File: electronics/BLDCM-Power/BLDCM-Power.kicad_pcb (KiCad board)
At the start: 4 copper layers, 32 x 32 mm, 48 parts, among them J1 501920-3001, J2 53048-0310, J3 505578-0460, J4 505578-0460, J5 FTSH-107-01-L-DV-K, J6 12402012E212A, U1 INA240A1PWR, U2 LDLN030G33R, U3 TMC6300-LA, U4 INA240A1PWR, U5 TCAN1462, U6 INA240A1PWR, U7 BAT54S, U8 LDO40LPU50RY, U9 TPS2115ADRB

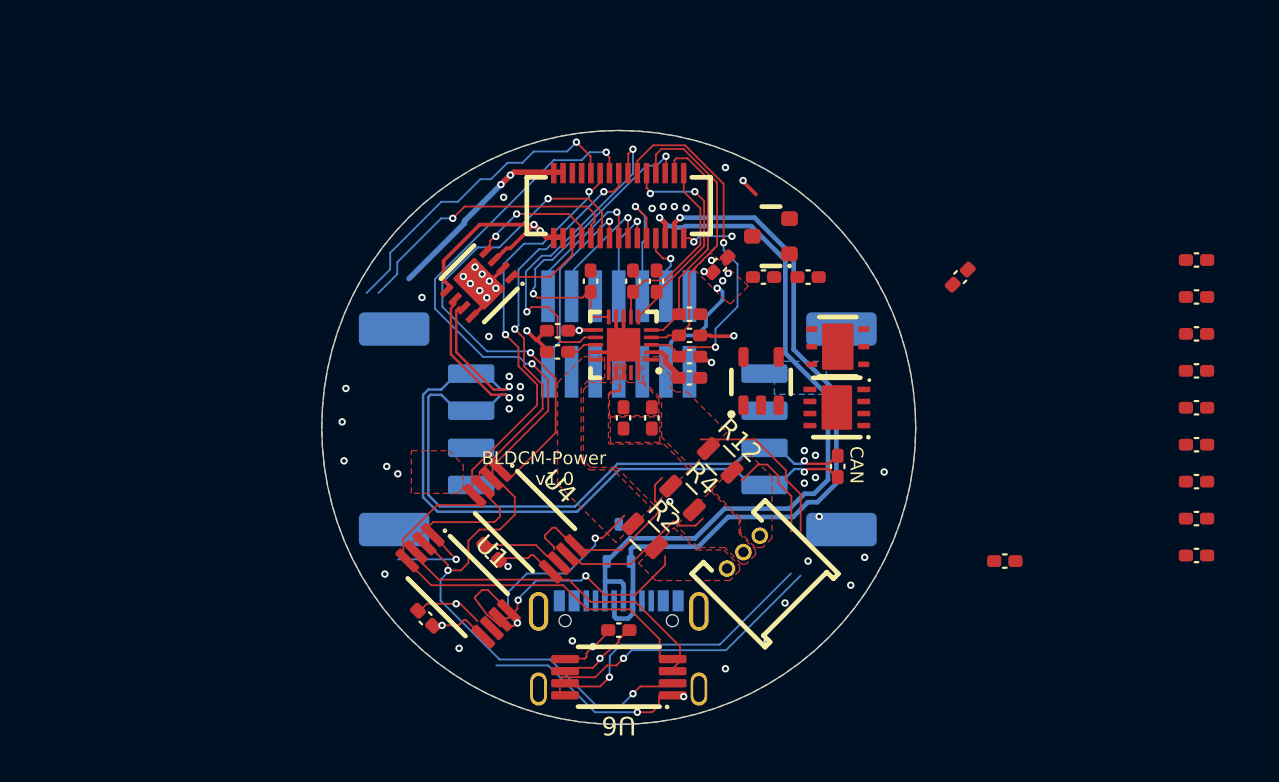
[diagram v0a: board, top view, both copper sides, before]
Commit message: Feat(schematic): High frequency voltage sense
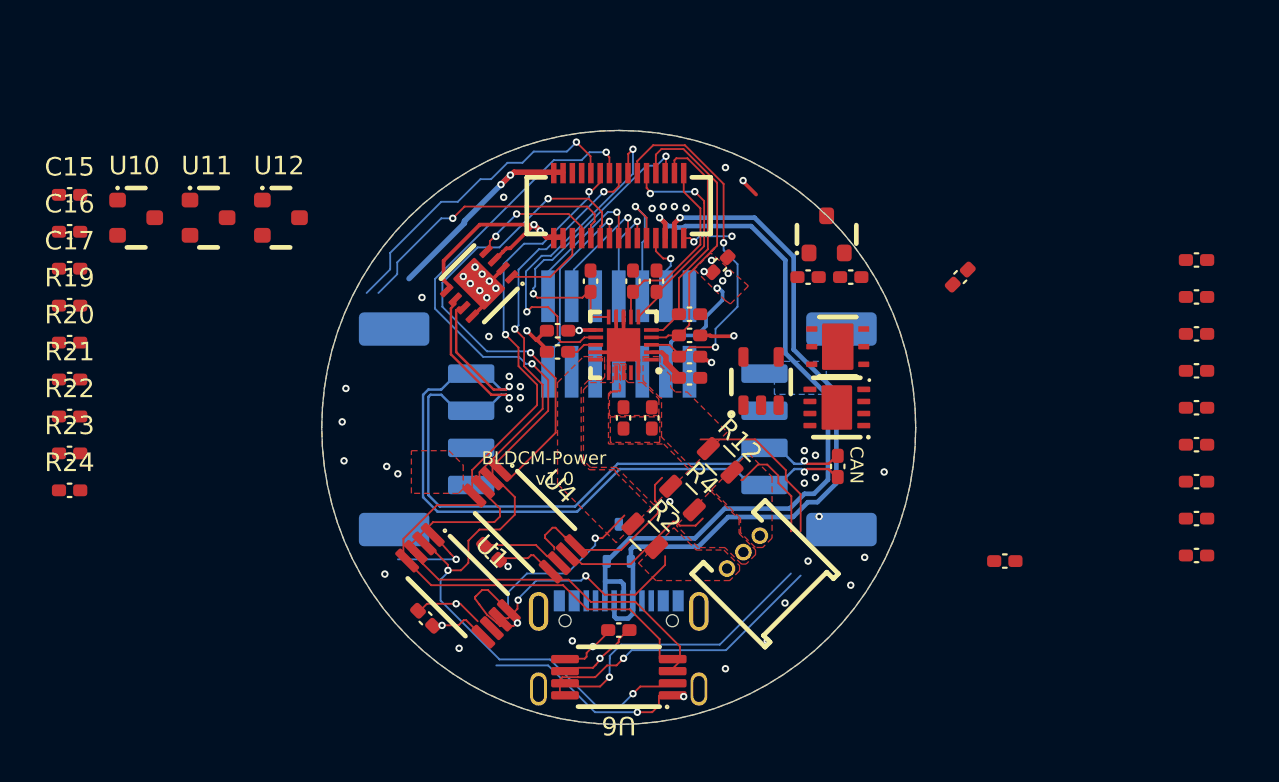
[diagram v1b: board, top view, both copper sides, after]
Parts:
- added C15: 10nF, BrenoCQ:C_0402, F.Cu at (118.9, 92.5)
- added C16: 10nF, BrenoCQ:C_0402, F.Cu at (118.9, 94.5)
- added C17: 10nF, BrenoCQ:C_0402, F.Cu at (118.9, 96.5)
- added R19: 20K, BrenoCQ:R_0402, F.Cu at (118.9, 98.4)
- added R20: 10K, BrenoCQ:R_0402, F.Cu at (118.9, 100.4)
- added R21: 20K, BrenoCQ:R_0402, F.Cu at (118.9, 102.4)
- added R22: 10K, BrenoCQ:R_0402, F.Cu at (118.9, 104.4)
- added R23: 20K, BrenoCQ:R_0402, F.Cu at (118.9, 106.4)
- added R24: 10K, BrenoCQ:R_0402, F.Cu at (118.9, 108.4)
- added U10: BAT54S, BrenoCQ:SOT-23, F.Cu at (122.5, 93.7)
- added U11: BAT54S, BrenoCQ:SOT-23, F.Cu at (126.4, 93.7)
- added U12: BAT54S, BrenoCQ:SOT-23, F.Cu at (130.3, 93.7)
- moved R1 4.70 mm to (161.0, 96.9)
- moved U7 3.00 mm to (159.7, 94.6), turned to 90 degrees
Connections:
- net /VOLT renamed /VOLT.SRC
- J1 pad 10: /INA.CS2 -> /INA.U
- J1 pad 11: /INA.CS1 -> /VOLT.W
- J1 pad 12: /INA.CLK -> /INA.V
- J1 pad 14: /INA.PICO -> /INA.W
- J1 pad 16: /INA.POCI -> /VOLT.U
- J1 pad 9: /INA.CS0 -> /VOLT.V
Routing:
- net (no net): track 0.00 -> 180.3 mm
- net /INA.PICO: track 54.7 -> 0.00 mm, vias 4 -> 0
- net /INA.POCI: track 48.3 -> 0.00 mm, vias 2 -> 0
- net /INA.CLK: track 45.4 -> 0.00 mm, vias 2 -> 0
- net /INA.CS1: track 27.6 -> 0.00 mm, vias 2 -> 0
- net /INA.CS0: track 19.7 -> 0.00 mm, vias 2 -> 0
- net /INA.U: track 0.00 -> 17.1 mm, vias 0 -> 1
- net /INA.CS2: track 17.1 -> 0.00 mm, vias 1 -> 0
- net /VOLT.V: track 0.00 -> 15.4 mm, vias 0 -> 2
- net /VOLT.W: vias 0 -> 2
- net /VOLT.U: vias 0 -> 2
- net /INA.W: vias 0 -> 4
- net /INA.V: vias 0 -> 2

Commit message: Feat(pcb): Route phase voltage sense
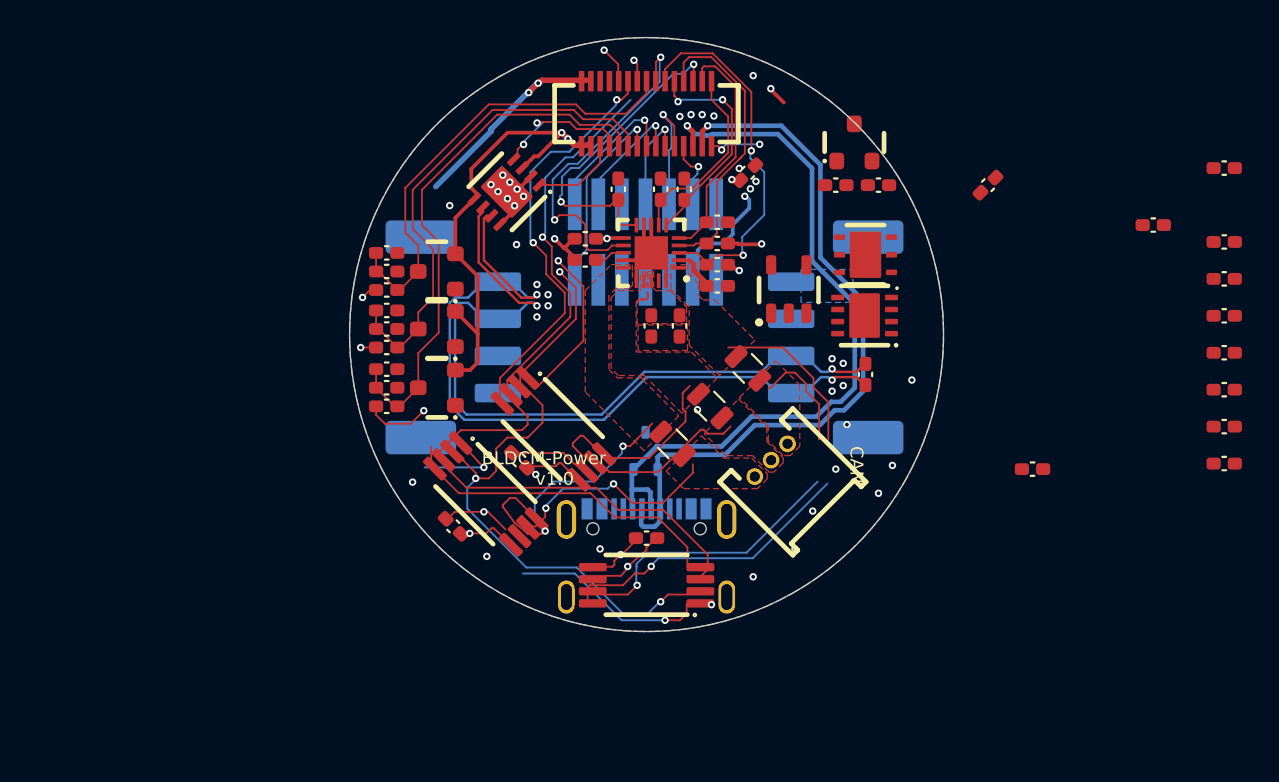
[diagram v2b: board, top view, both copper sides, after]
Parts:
- moved C15 19.5 mm to (136.0, 101.9), turned to 180 degrees
- moved R24 19.2 mm to (136.0, 99.7), turned to 180 degrees
- moved R23 18.0 mm to (136.0, 100.7), turned to 180 degrees
- moved C16 17.6 mm to (136.0, 98.7), turned to 180 degrees
- moved R20 17.5 mm to (136.0, 96.6), turned to 180 degrees
- moved R22 17.2 mm to (136.0, 102.9), turned to 180 degrees
- moved R21 17.1 mm to (136.0, 103.9), turned to 180 degrees
- moved C17 17.1 mm to (136.0, 95.6), turned to 180 degrees
- moved R19 17.1 mm to (136.0, 97.6), turned to 180 degrees
- moved U10 16.5 mm to (138.7, 96.6), turned to 180 degrees
- moved U11 15.3 mm to (138.7, 102.9), turned to 180 degrees
- moved U12 10.3 mm to (138.7, 99.7), turned to 180 degrees
- moved J1 5.18 mm to (150.0, 88.1)
- moved J6 5.18 mm to (150.0, 114.1)
- moved C4 5.17 mm to (155.5, 91.3)
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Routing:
- net (no net): track 180.3 -> 131.5 mm
- net /VOLT.W: track 0.00 -> 27.0 mm, vias 2 -> 1
- net /VOLT.U: track 0.00 -> 25.0 mm, vias 2 -> 1
- net /INA.U: track 17.1 -> 1.95 mm
- net /VOLT.V: track 15.4 -> 28.9 mm, vias 2 -> 1
- net 3.3V: track 28.7 -> 41.5 mm
- net /TMC.V.OUT: track 9.32 -> 12.8 mm, vias 0 -> 1
- net /INA.V: track 10.7 -> 12.1 mm
- net /INA.W: track 0.00 -> 1.20 mm
- net /TMC.U.OUT: track 12.3 -> 13.2 mm, vias 2 -> 3
- net /TMC.W.OUT: track 20.6 -> 21.4 mm, vias 1 -> 2
- net GND: vias 44 -> 38
- removed copper zone on F.Cu, net 3.3V
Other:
- outline, holes or cut-outs redrawn

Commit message: Feat(pcb): Route power management
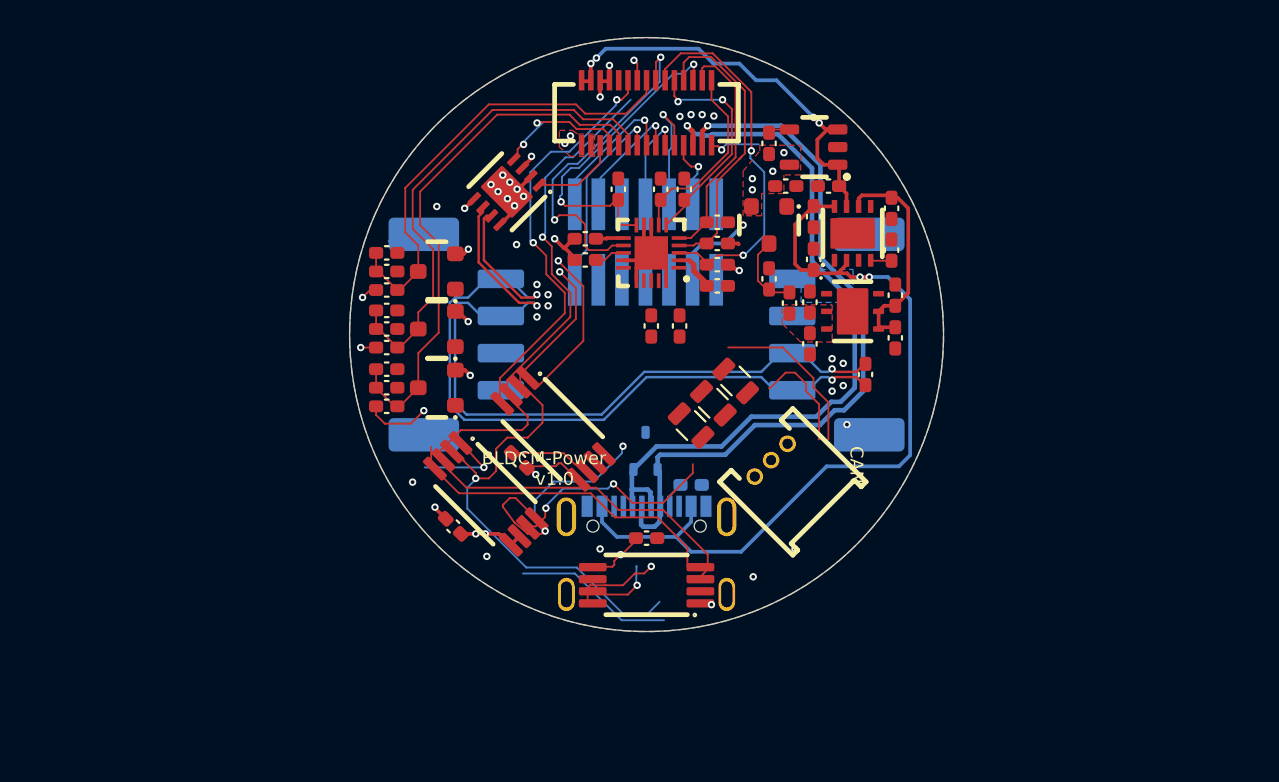
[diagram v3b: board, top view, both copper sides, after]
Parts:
- R3: moved to B.Cu
- moved R14 26.2 mm to (156.6, 89.7), turned to 90 degrees
- moved R17 24.8 mm to (159.0, 93.7), turned to -90 degrees
- moved C11 23.5 mm to (158.8, 98.2), turned to -90 degrees
- moved R16 22.5 mm to (158.8, 100.5), turned to -90 degrees
- moved C14 22.1 mm to (159.0, 96.0), turned to 90 degrees
- moved R18 19.0 mm to (163.4, 100.2), turned to -90 degrees
- moved R15 18.8 mm to (163.2, 95.5), turned to 90 degrees
- moved R3 18.4 mm to (152.4, 108.1), turned to 180 degrees
- moved C13 18.0 mm to (163.2, 93.2), turned to -90 degrees
- moved C12 14.4 mm to (163.4, 97.9), turned to -90 degrees
- moved C3 8.60 mm to (159.8, 92.0), turned to 0 degrees
- moved R1 7.96 mm to (157.7, 98.3), turned to -90 degrees
- moved U2 7.77 mm to (159.0, 89.9), turned to 90 degrees
- moved U7 6.40 mm to (156.6, 94.1), turned to -90 degrees
- moved R13 6.20 mm to (156.6, 97.0), turned to -90 degrees
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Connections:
- net Net-(U8-SENSE) renamed /Power Management/VIN_5V
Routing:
- net VBUS: track 0.00 -> 43.4 mm, vias 0 -> 2
- net 3.3V: track 41.5 -> 20.0 mm, vias 11 -> 16
- net /Power Management/VIN_5V: track 0.00 -> 11.9 mm
- net 5V: track 11.5 -> 23.2 mm, vias 2 -> 4
- net /TMC.W.OUT: track 21.4 -> 9.66 mm
- net /TMC.W.IN: track 26.0 -> 14.6 mm
- net /INA.V: track 12.1 -> 1.40 mm
- net /TMC.V.OUT: track 12.8 -> 3.52 mm
- net GND: track 27.0 -> 21.6 mm, vias 38 -> 31
- net /VOLT.SRC: track 2.81 -> 7.02 mm, vias 2 -> 1
- net /TMC.U.IN: track 14.9 -> 12.8 mm
- net /INA.U: track 1.95 -> 0.00 mm, vias 1 -> 0
- net unconnected-(U6-NC-Pad1): track 10.5 -> 8.65 mm, vias 2 -> 1
- net (no net): track 131.5 -> 129.9 mm
- net Net-(J6-CC1): track 0.00 -> 1.53 mm
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- added copper zone on F.Cu, net 3.3V
- removed copper zone on F.Cu, net /TMC.U.IN
- removed copper zone on F.Cu, net /TMC.U.OUT
- removed copper zone on F.Cu, net /TMC.V.IN
- removed copper zone on F.Cu, net /TMC.V.OUT
- removed copper zone on F.Cu, net /TMC.W.IN
- removed copper zone on F.Cu, net /TMC.W.OUT

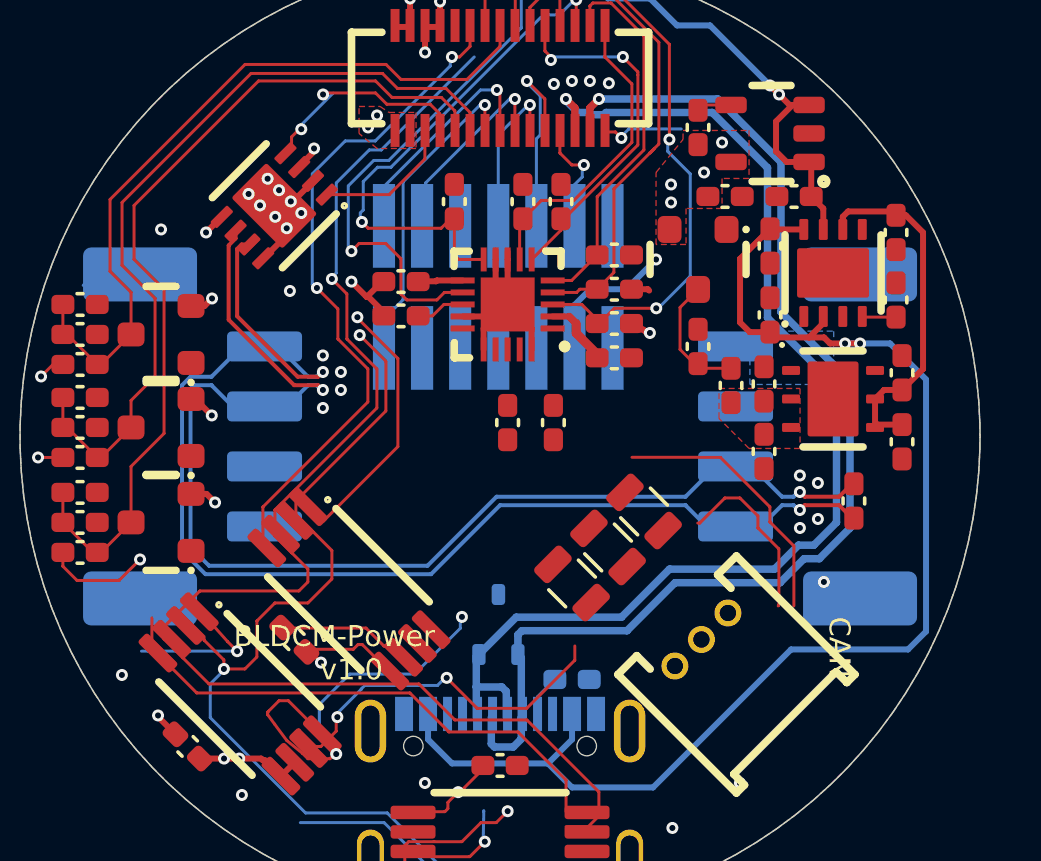
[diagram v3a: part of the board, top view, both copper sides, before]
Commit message: Feat(pcb): Route motor phases
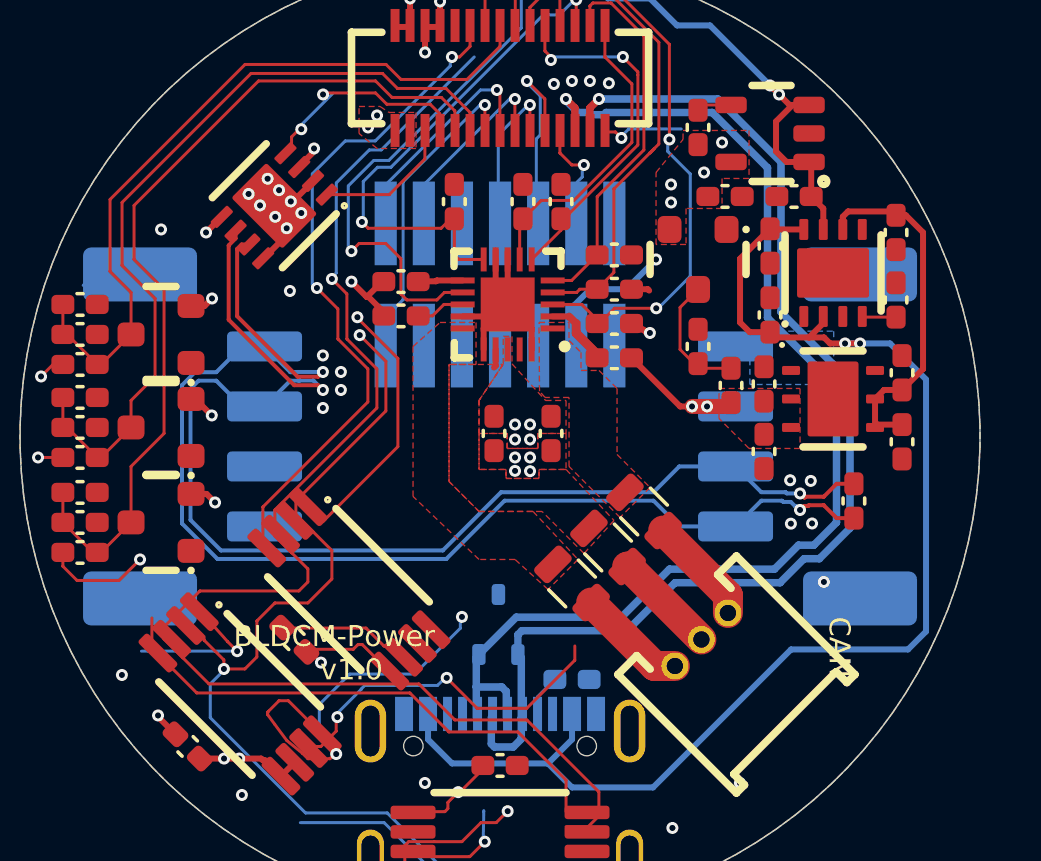
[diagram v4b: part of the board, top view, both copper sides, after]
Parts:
- moved C9 0.58 mm to (149.8, 99.9)
- moved C10 0.37 mm to (151.7, 99.9)
- moved J5 0.10 mm to (150.0, 95.0)
- turned R11 to -90 degrees
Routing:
- net /TMC.W.IN: track 14.6 -> 5.68 mm
- net VIN: track 16.3 -> 20.2 mm, vias 0 -> 6
- net /TMC.U.OUT: track 13.2 -> 16.8 mm
- net /TMC.V.OUT: track 3.52 -> 7.00 mm
- net /TMC.W.OUT: track 9.66 -> 7.41 mm
- net /CAN.DP: track 42.2 -> 41.4 mm
- net /CAN.DN: track 41.9 -> 41.2 mm
- net /TMC.V.IN: track 0.00 -> 0.62 mm
- net GND: vias 31 -> 35
- added copper zone on F.Cu, net /TMC.U.IN
- added copper zone on F.Cu, net /TMC.V.IN
- added copper zone on F.Cu, net /TMC.W.IN
